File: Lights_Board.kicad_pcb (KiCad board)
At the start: 2 copper layers, 100 x 100 mm, 72 parts, among them J1 Conn_ARM_JTAG_SWD_10, J2 USB_B_Micro, J3 34830-0801, J6 34830-0801, J7 34830-0801, J8 34830-0801, Q1 AO3400A, Q2 AO3400A, Q3 AO3400A, Q4 AO3400A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

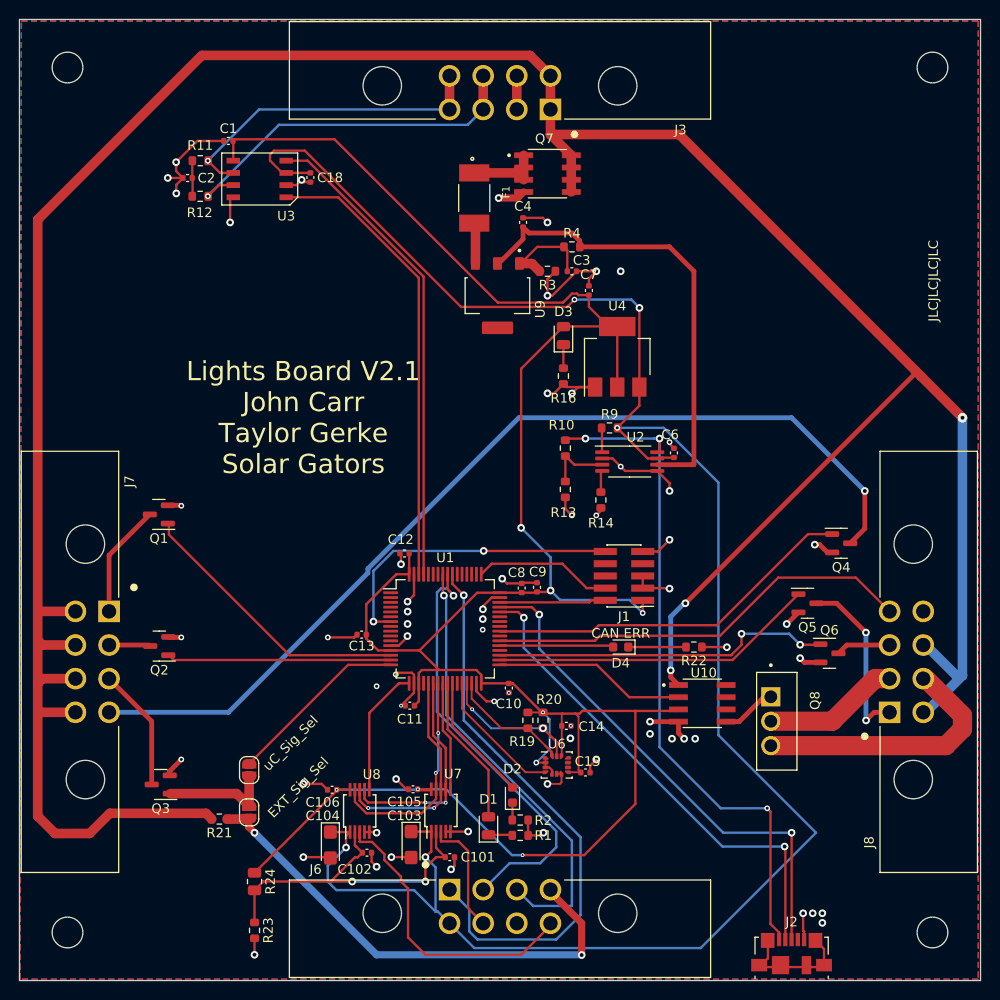
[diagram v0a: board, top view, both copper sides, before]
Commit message: FSGP 2023 Lights Hardware
Final PCB revision used for Sunrider at FSGP 2023
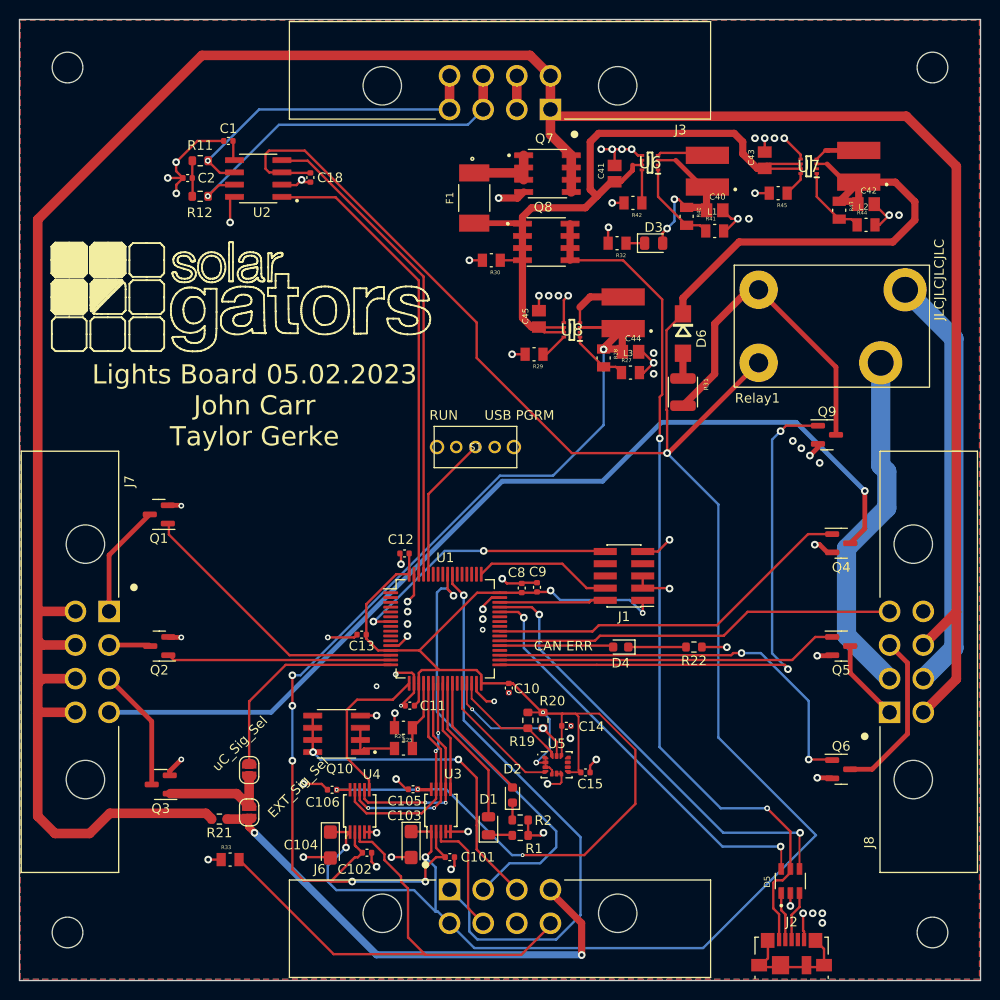
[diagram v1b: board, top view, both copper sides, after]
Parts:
- removed C3, C4: 10uF, Capacitor_SMD:C_0402_1005Metric
- removed C6, C7: 1uF, Capacitor_SMD:C_0402_1005Metric
- removed R10, R13, R16, R9: 10k, Resistor_SMD:R_0603_1608Metric
- removed R14: 220, Resistor_SMD:R_0603_1608Metric
- removed R23: 2.15k, Resistor_SMD:R_0603_1608Metric
- removed R24: 1.8k, Resistor_SMD:R_0805_2012Metric
- removed R3: 15k, Resistor_SMD:R_0603_1608Metric
- removed R4: 5.1k, Resistor_SMD:R_0603_1608Metric
- removed U10: IR2104STRPBF, AO4407A (1):SOIC127P600X175-8N
- removed the U3 at (125.0, 66.6)
- removed the U4 at (162.2, 85.1)
- removed U9: AMS1117, AMS1117 (1):SOT229P700X180-4N
- added C40: CL21A226MAQNNNE, CL21A226MAQNNNE:CAPC2012X140N, F.Cu at (172.3, 69.8)
- added C41: CL21A226MAQNNNE, CL21A226MAQNNNE:CAPC2012X140N, F.Cu at (161.9, 66.0)
- added C42: CL21A226MAQNNNE, CL21A226MAQNNNE:CAPC2012X140N, F.Cu at (188.1, 69.2)
- added C43: CL21A226MAQNNNE, CL21A226MAQNNNE:CAPC2012X140N, F.Cu at (177.5, 64.6)
- added C44: CL21A226MAQNNNE, CL21A226MAQNNNE:CAPC2012X140N, F.Cu at (163.6, 84.6)
- added C45: CL21A226MAQNNNE, CL21A226MAQNNNE:CAPC2012X140N, F.Cu at (154.1, 81.2)
- added D5: USBLC6-2SC6, USBLC6-2SC6:SOT95P280X145-6N, F.Cu at (180.2, 139.6)
- added D6: SS54, SS54:DO-214AC, F.Cu at (169.0, 82.7)
- added L1: LVS505040-2R2M-N, SDR0403-2R2ML:IND_SDR0403-2R2ML, F.Cu at (171.6, 65.8)
- added L2: LVS505040-2R2M-N, SDR0403-2R2ML:IND_SDR0403-2R2ML, F.Cu at (187.3, 65.3)
- added L3: LVS505040-2R2M-N, SDR0403-2R2ML:IND_SDR0403-2R2ML, F.Cu at (162.8, 80.5)
- added Q10: AO4407A, AO4407A (1):SOIC127P600X175-8N, F.Cu at (133.0, 124.3)
- added Q9: AO3400A, Package_TO_SOT_SMD:SOT-23, F.Cu at (184.0, 93.2)
- added R25: 0805W8F1003T5E, CR0805AJ_-000EAS:RESC2012X60N, F.Cu at (140.0, 123.7)
- added R26: 0805W8F3573T5E, CR0805AJ_-000EAS:RESC2012X60N, F.Cu at (140.0, 125.9)
- added R27: CR0805F83402G, CR0805AJ_-000EAS:RESC2012X60N, F.Cu at (163.6, 86.7)
- added R28: 0805W8F6812T5E, CR0805AJ_-000EAS:RESC2012X60N, F.Cu at (160.8, 85.2)
- added R29: WR08X9311FTL, CR0805AJ_-000EAS:RESC2012X60N, F.Cu at (153.5, 84.8)
- added R30: 0805W8F1803T5E, CR0805AJ_-000EAS:RESC2012X60N, F.Cu at (149.1, 75.1)
- added R31: 1210W2F232KT5E, 3-1879463-6:RESC3125X65N, F.Cu at (169.0, 88.8)
- added R32: 0805W8F1801T5E, CR0805AJ_-000EAS:RESC2012X60N, F.Cu at (162.2, 73.3)
- added R33: 0805W8F6800T5E, CR0805AJ_-000EAS:RESC2012X60N, F.Cu at (121.9, 137.4)
- added R40: WR08X2493FTL, CR0805AJ_-000EAS:RESC2012X60N, F.Cu at (169.4, 70.5)
- added R41: CR0805F83402G, CR0805AJ_-000EAS:RESC2012X60N, F.Cu at (172.3, 72.0)
- added R42: WR08X9311FTL, CR0805AJ_-000EAS:RESC2012X60N, F.Cu at (163.8, 69.1)
- added R43: HPCR0805F249KK9, CR0805AJ_-000EAS:RESC2012X60N, F.Cu at (185.3, 69.8)
- added R44: CR0805F83402G, CR0805AJ_-000EAS:RESC2012X60N, F.Cu at (188.1, 71.4)
- added R45: WR08X9311FTL, CR0805AJ_-000EAS:RESC2012X60N, F.Cu at (178.9, 68.1)
- added Relay1: AHQSS105DM2FA0G, FUSE_1812L200_12DR:AHQSS105DM2FA0G, F.Cu at (176.9, 85.7)
- added S1: 1825232-1, 1825232-1:1825232-1, F.Cu at (147.4, 94.5)
- added U5: LSM6DS3, Package_LGA:LGA-14_3x2.5mm_P0.5mm_LayoutBorder3x4y, F.Cu at (155.9, 127.5)
- added U7: TPS629206QDRLRQ1, SamacSys_Parts:SOTFL50P160X60-8N, F.Cu at (182.1, 65.3)
- added U8: TPS629206QDRLRQ1, SamacSys_Parts:SOTFL50P160X60-8N, F.Cu at (157.5, 82.3)
- D3: value Brd_ON -> Board OK
- F1: value SMD1812P300TF -> SMD1812P075TF/24
- Q8: value IRFZ44NPBF -> AO4407A; footprint LightsHardware-main:TO254P1016X419X2286-3 -> AO4407A (1):SOIC127P600X175-8N
- U2: value TPS2113 -> TCAN1042xV; footprint Package_SO:TSSOP-8_4.4x3mm_P0.65mm -> TCAN1042VDQ1:SOIC127P599X175-8N
- U6: value LSM6DS3 -> TPS629206QDRLRQ1; footprint Package_LGA:LGA-14_3x2.5mm_P0.5mm_LayoutBorder3x4y -> SamacSys_Parts:SOTFL50P160X60-8N
- moved U6 63.4 mm to (165.6, 64.9), turned to 180 degrees
- moved Q8 55.1 mm to (154.8, 73.2), turned to 0 degrees
- moved U2 48.6 mm to (124.8, 66.5), turned to 180 degrees
- moved D3 13.4 mm to (166.0, 73.3), turned to 0 degrees
- moved Q6 12.1 mm to (185.5, 128.0)
- moved Q5 5.67 mm to (185.5, 115.2)
- renumbered U7 to U3, U8 to U4
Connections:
- J2 pad 2: /D- -> /D-_USB
- J2 pad 3: /D+ -> /D+_USB
- J6 pad 3: /Aux_C3 -> /sup_batt_in
- Q8 pad 1: Net-(U10-Pad5) -> /12V_safe
- Q8 pad 2: /HORN1 -> /12V_safe
- Q8 pad 3: /HORN2 -> /12V_safe
- U1 pad 20: unconnected-(U1-Pad20) -> /sup_batt_div
- U1 pad 57: /Aux_C3 -> unconnected-(U1-Pad57)
- U1 pad 60: unconnected-(U1-Pad60) -> /BOOT
- U2 pad 1: /PWR_STAT -> /TXD
- U2 pad 3: /VSNS -> +5V
- U2 pad 4: Net-(R14-Pad1) -> /RXD
- U2 pad 5: GND -> +3V3
- U2 pad 6: /5v_Reg -> /CAN-
- U2 pad 7: +5V -> /CAN+
- U2 pad 8: /5v_USB -> GND
- U6 pad 1: +3V3 -> Net-(R40-Pad2)
- U6 pad 2: +3V3 -> unconnected-(U6-Pad2)
- U6 pad 4: /INT1_IMU -> Net-(L1-Pad2)
- U6 pad 5: +3V3 -> GND
- U6 pad 6: GND -> /12V_safe
- U6 pad 7: GND -> /12V_safe
- U6 pad 8: +3V3 -> Net-(R42-Pad1)
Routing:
- net +3V3: track 259.9 -> 167.2 mm, vias 8 -> 9
- net +1V8: track 35.5 -> 111.8 mm, vias 2 -> 6
- net /12V_safe: track 4.50 -> 76.6 mm
- net +5V: track 203.1 -> 265.8 mm, vias 5 -> 3
- net /5v_Reg: track 49.0 -> 0.00 mm
- net /Aux_C3: track 46.5 -> 0.00 mm, vias 1 -> 0
- net /HORN_EN: track 20.0 -> 60.1 mm, vias 0 -> 2
- net /sup_batt_in: track 0.00 -> 35.3 mm, vias 0 -> 2
- net Net-(Q9-Pad3): track 0.00 -> 34.4 mm
- net +12V: track 309.0 -> 280.3 mm, vias 3 -> 0
- net /Break: track 30.9 -> 54.3 mm
- net /HORN1: track 14.2 -> 36.7 mm
- net /5v_USB: track 71.4 -> 91.7 mm, vias 3 -> 2
- net /HORN2: track 27.7 -> 43.9 mm
- net /BOOT: track 0.00 -> 15.3 mm
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- added copper zone on F.Cu, net +3V3
- removed copper zone on F.Cu, net GND
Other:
- board text added: "."
- board text added: "Lights Board 05.02.2023 John Carr Taylor Gerke"
- board text added: "RUN"
- board text added: "USB PGRM"
- board text removed: "Lights Board V2.1 John Carr Taylor Gerke Solar Gators"
